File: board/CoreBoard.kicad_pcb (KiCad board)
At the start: 2 copper layers, 121.4 x 88.9 mm, 98 parts, among them J1 RJ45_LED_Shielded, J2 768250002, Q1 AO3401A, Q10 AO3401A, Q11 AO3401A, Q2 AO3401A, Q3 AO3401A, Q4 AO3401A, Q5 AO3401A, Q6 AO3401A, Q7 AO3401A, Q8 AO3401A, Q9 AO3401A, SW11 SW_Wuerth_450301014042, SW12 SW_Wuerth_450301014042, SW13 SW_Wuerth_450301014042, SW14 SW_Wuerth_450301014042, SW15 SW_Wuerth_450301014042, SW16 SW_Wuerth_450301014042, SW4 SW_Push, SW6 SW_Push, SW7 SW_Push, SW8 SW_Push, U1 74VHC138FT, U2 OKI-78SR-12_1.0-W36H-C, U3 SHHD003A0A, U4 GY-521, U5 Teensy4.1_DEV-16771, U6 MCP9808-E/MS

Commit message: rev2 progress
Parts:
- removed R28, R29: 10k, Resistor_SMD:R_0603_1608Metric_Pad0.98x0.95mm_HandSolder
- removed U3: SHHD003A0A, MRDT_Devices:SHHD003A0A-SRZ_Surface_Mount
- added C4: 10µF, Capacitor_SMD:C_1206_3216Metric_Pad1.33x1.80mm_HandSolder, F.Cu at (98.6, 91.4)
- added C5: 10µF, Capacitor_SMD:C_0603_1608Metric_Pad1.08x0.95mm_HandSolder, F.Cu at (97.7, 94.4)
- added Q1: AO3401A, Package_TO_SOT_SMD:SOT-23, F.Cu at (40.7, 78.7)
- added Q10: AO3401A, Package_TO_SOT_SMD:SOT-23, F.Cu at (50.5, 83.3)
- added Q12: AO3401A, Package_TO_SOT_SMD:SOT-23, F.Cu at (50.5, 87.9)
- added Q16: BSS138, Package_TO_SOT_SMD:SOT-23, F.Cu at (136.7, 121.5)
- added Q17: BSS138, Package_TO_SOT_SMD:SOT-23, F.Cu at (141.2, 121.9)
- added Q18: BSS138, Package_TO_SOT_SMD:SOT-23, F.Cu at (145.3, 121.9)
- added Q2: AO3401A, Package_TO_SOT_SMD:SOT-23, F.Cu at (40.7, 83.3)
- added Q3: AO3401A, Package_TO_SOT_SMD:SOT-23, F.Cu at (40.7, 87.9)
- added Q4: AO3401A, Package_TO_SOT_SMD:SOT-23, F.Cu at (40.7, 92.6)
- added Q5: AO3401A, Package_TO_SOT_SMD:SOT-23, F.Cu at (45.6, 78.7)
- added Q6: AO3401A, Package_TO_SOT_SMD:SOT-23, F.Cu at (45.6, 83.3)
- added Q7: AO3401A, Package_TO_SOT_SMD:SOT-23, F.Cu at (45.6, 87.9)
- added Q8: AO3401A, Package_TO_SOT_SMD:SOT-23, F.Cu at (45.6, 92.6)
- added Q9: AO3401A, Package_TO_SOT_SMD:SOT-23, F.Cu at (50.5, 78.7)
- added R17: 10k, Resistor_SMD:R_0603_1608Metric_Pad0.98x0.95mm_HandSolder, F.Cu at (138.8, 117.3)
- added R19: 10k, Resistor_SMD:R_0603_1608Metric_Pad0.98x0.95mm_HandSolder, F.Cu at (141.3, 117.3)
- added U7: OKI-78SR-5_1.5-W36H-C, Converter_DCDC:Converter_DCDC_Murata_OKI-78SR_Horizontal, F.Cu at (89.8, 89.9)
- MOSFET1: footprint MRDT_Devices:SOP-8_TOS-L -> CoreBoard:MSOP8_MC_MCH-L
- R27: value 6.8k -> 10k
- moved H4 21.8 mm to (168.7, 135.6)
- moved R16 5.24 mm to (192.0, 118.4)
- moved J1 5.11 mm to (181.5, 142.1)
- moved R27 2.17 mm to (143.8, 117.3)
- moved Conn9 1.55 mm to (144.3, 126.5)
- moved R14 1.05 mm to (192.0, 121.9)
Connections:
- Conn9 pad 1: /Fans/PWM2 -> +5V
- Conn9 pad 3: +12V -> Net-(Q17-D)
- Conn9 pad 4: GND -> Net-(Q18-D)
- R27 pad 1: /Fans/Tach2 -> /Lighting/BStrip
- U5 pad 33: unconnected-(U5-MCLK2-Pad33) -> /Lighting/GStrip
- U5 pad 4: /Fans/Tach2 -> /Lighting/RStrip
- U5 pad 9: /Fans/PWM2 -> /Lighting/BStrip
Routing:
- net /Lighting/GStrip: track 0.00 -> 211.0 mm, vias 0 -> 1
- net /Lighting/RStrip: track 0.00 -> 74.1 mm, vias 0 -> 5
- net /Lighting/BStrip: track 0.00 -> 70.6 mm, vias 0 -> 5
- net /Fans/PWM2: track 68.1 -> 0.00 mm, vias 5 -> 0
- net /Fans/Tach2: track 54.8 -> 0.00 mm, vias 3 -> 0
- net Rx-: track 41.8 -> 69.2 mm
- net Net-(Q18-D): track 0.00 -> 23.8 mm, vias 0 -> 1
- net /Accelerometer/AccSDA: track 117.6 -> 96.9 mm, vias 4 -> 3
- net /Accelerometer/AccSCL: track 126.0 -> 105.5 mm, vias 3 -> 2
- net Net-(Q17-D): track 0.00 -> 19.3 mm, vias 0 -> 2
- net Rx+: track 41.7 -> 58.3 mm
- net VCC: track 60.2 -> 76.6 mm, vias 2 -> 5
- net +3.3V: track 401.1 -> 411.7 mm, vias 12 -> 11
- net Net-(Q16-D): track 12.7 -> 6.72 mm
- net Tx+: track 28.0 -> 33.6 mm, vias 0 -> 1
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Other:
- board text removed: "Fan2"

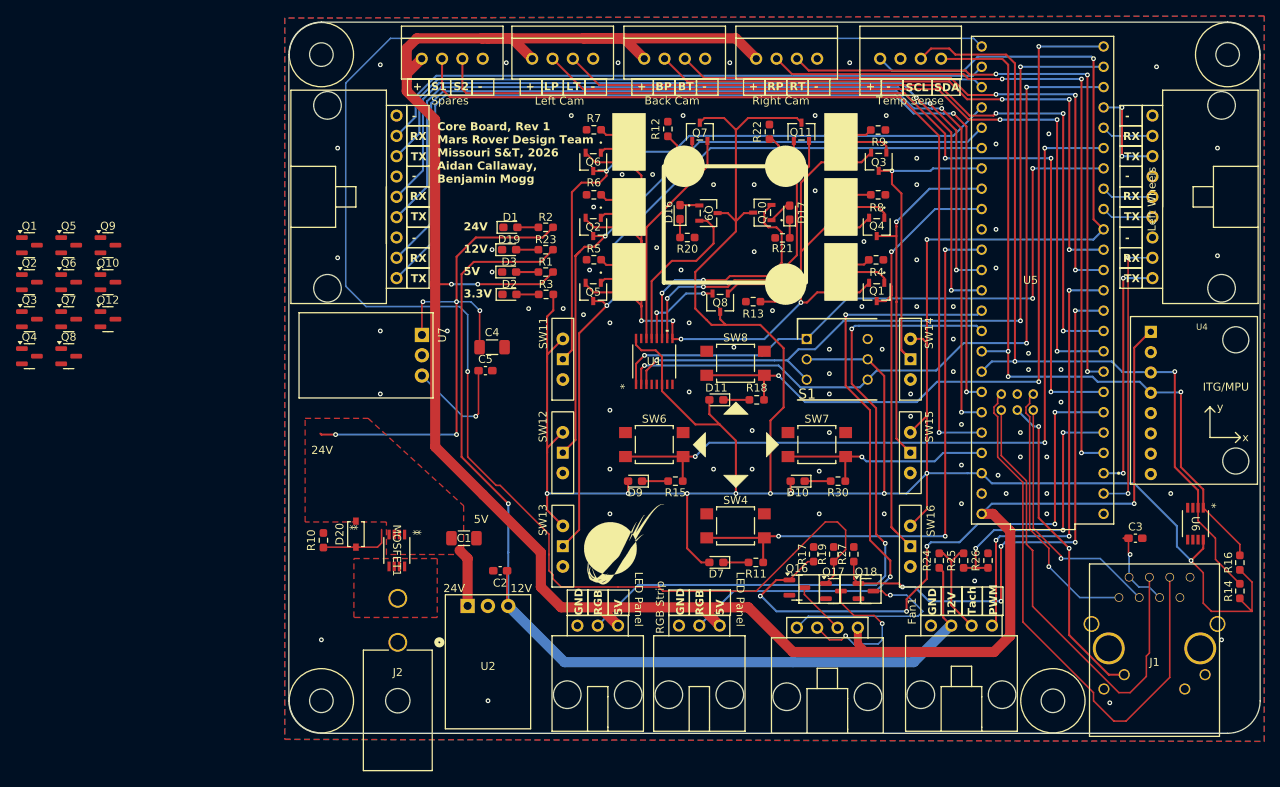
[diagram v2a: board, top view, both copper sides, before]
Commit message: move things for buck circuit
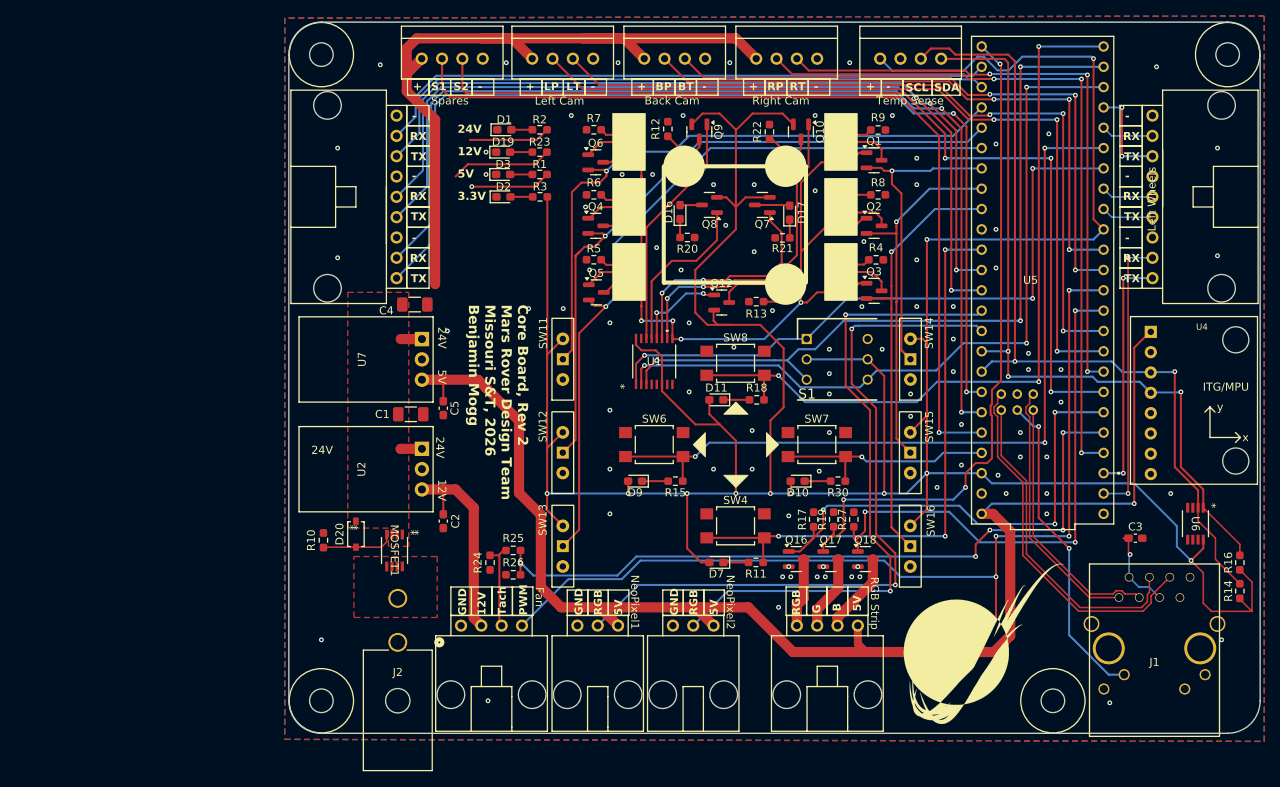
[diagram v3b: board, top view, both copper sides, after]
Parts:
- removed the G*** at (115.1, 116.1)
- removed the Q1 at (146.6, 84.5)
- removed the Q10 at (132.3, 74.6)
- removed Q11: AO3401A, CoreBoard:SOT-23-3L_AOS-L
- removed the Q2 at (111.2, 76.4)
- removed the Q3 at (146.9, 68.2)
- removed the Q4 at (146.6, 76.4)
- removed the Q5 at (111.2, 84.5)
- removed the Q6 at (111.2, 68.3)
- removed the Q7 at (124.5, 64.5)
- removed the Q8 at (127.1, 85.9)
- removed the Q9 at (125.6, 74.7)
- added G***: LOGO, MRDT_Silkscreens:0_MRDT_Logo_20mm, F.Cu at (160.0, 128.5)
- moved Q1 106.1 mm to (146.3, 68.1)
- moved Q2 105.8 mm to (146.3, 76.3)
- moved Q3 105.6 mm to (146.3, 84.4)
- moved Q10 88.6 mm to (137.2, 64.5), turned to -90 degrees
- moved Q7 87.9 mm to (132.3, 73.7), turned to 180 degrees
- moved Q8 82.3 mm to (125.7, 73.7), turned to 180 degrees
- moved Q12 76.7 mm to (127.3, 85.9)
- moved Q9 75.3 mm to (124.5, 64.5), turned to -90 degrees
- moved Q4 72.6 mm to (111.5, 76.3)
- moved Q6 67.6 mm to (111.5, 68.3)
- moved Q5 66.2 mm to (111.6, 84.6)
- moved R26 59.4 mm to (101.2, 119.9), turned to 180 degrees
- moved Conn2 58.7 mm to (102.3, 126.2)
- moved R25 56.3 mm to (101.2, 116.8), turned to 0 degrees
- moved R24 56.1 mm to (98.3, 118.4)
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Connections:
- C5 pad 1: +12V -> +5V
- Conn9 pad 2: Net-(Q16-D) -> Net-(Q18-D)
- Conn9 pad 4: Net-(Q18-D) -> Net-(Q16-D)
- U7 pad 3: +12V -> +5V
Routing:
- net /Lighting/GStrip: track 211.0 -> 84.2 mm, vias 1 -> 3
- net +12V: track 143.8 -> 38.3 mm, vias 2 -> 0
- net /Fans/PWM1: track 55.3 -> 119.0 mm, vias 3 -> 4
- net VCC: track 76.6 -> 15.5 mm, vias 5 -> 0
- net /Fans/Tach1: track 35.1 -> 92.1 mm, vias 3 -> 5
- net Rx-: track 69.2 -> 45.6 mm
- net +3.3V: track 411.7 -> 430.6 mm
- net Rx+: track 58.3 -> 40.6 mm
- net /Lighting/RStrip: track 74.1 -> 60.3 mm, vias 5 -> 3
- net Net-(Q18-D): track 23.8 -> 10.1 mm, vias 1 -> 0
- net Net-(Q17-D): track 19.3 -> 9.41 mm, vias 2 -> 0
- net +5V: track 286.5 -> 277.7 mm, vias 3 -> 2
- net /Lighting/BStrip: track 70.6 -> 67.7 mm, vias 5 -> 3
- net /Lighting/Lighting_Panel: track 87.8 -> 90.2 mm
- net /Selection LEDs/Spare2: track 31.3 -> 29.1 mm
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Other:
- board text added: "B"
- board text added: "Core Board, Rev 2 Mars Rover Design Team Missouri S&T, 2026 Benjamin Mogg"
- board text added: "Fan"
- board text added: "G"
- board text added: "NeoPixel1"
- board text added: "NeoPixel2"
- board text removed: "Core Board, Rev 1 Mars Rover Design Team Missouri S&T, 2026 Aidan Callaway, Benjamin Mogg"
- board text removed: "Fan1"
- board text removed: "LED Panel"

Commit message: add athena silkscreen
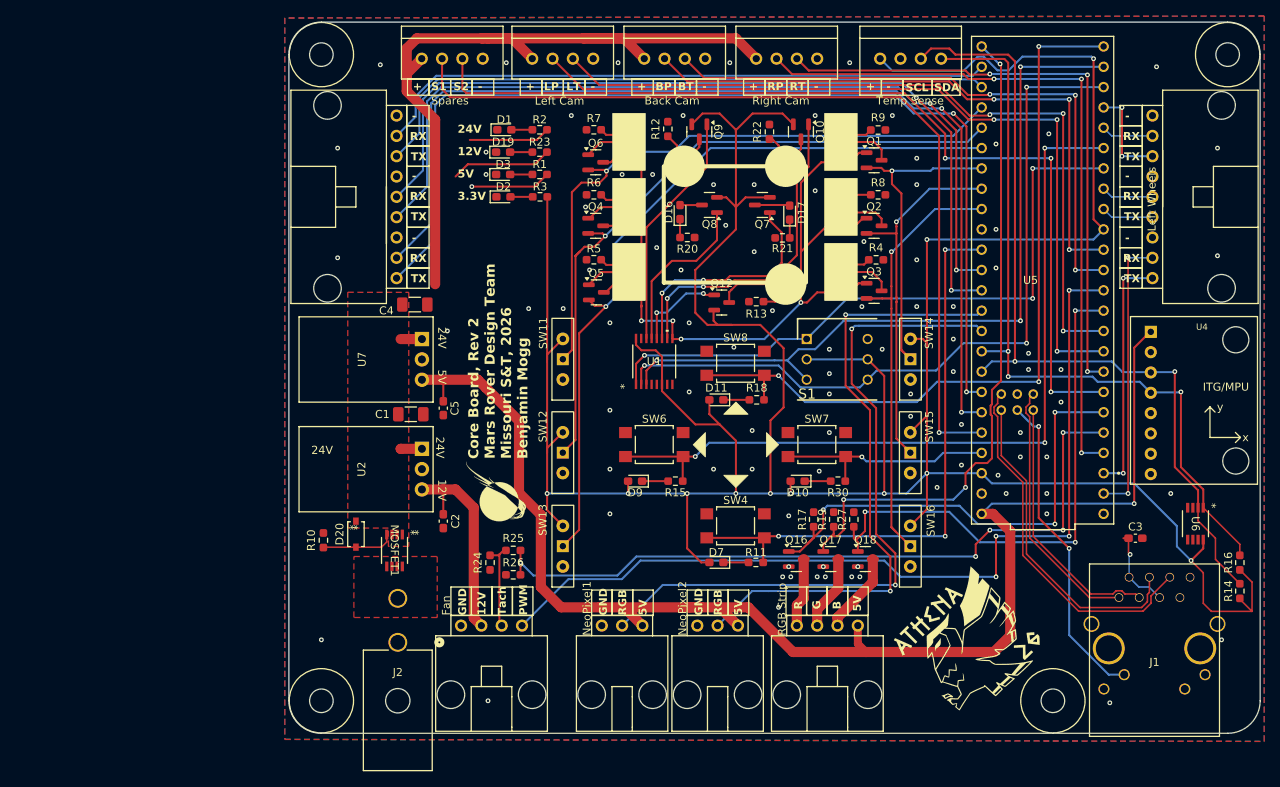
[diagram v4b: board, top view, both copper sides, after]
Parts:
- removed the G*** at (160.0, 128.5)
- added G***: LOGO, MRDT_Silkscreens:0_MRDT_Logo_7.5mm, F.Cu at (99.1, 109.5)
- added G***: LOGO, CoreBoard:Athena_Patch, F.Cu at (158.0, 128.5)
- moved Conn1 3.05 mm to (129.3, 126.2)
- moved Conn10 3.05 mm to (117.3, 126.2)
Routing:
- net /Fans/PWM1: track 119.0 -> 113.4 mm
- net /Lighting/RGB_Strip: track 80.5 -> 77.5 mm
- net /Lighting/Lighting_Panel: track 90.2 -> 87.2 mm
- net /Selection LEDs/Wheels: track 115.0 -> 114.1 mm
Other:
- board text added: "R"

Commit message: Add plated mounting holes and buck converter
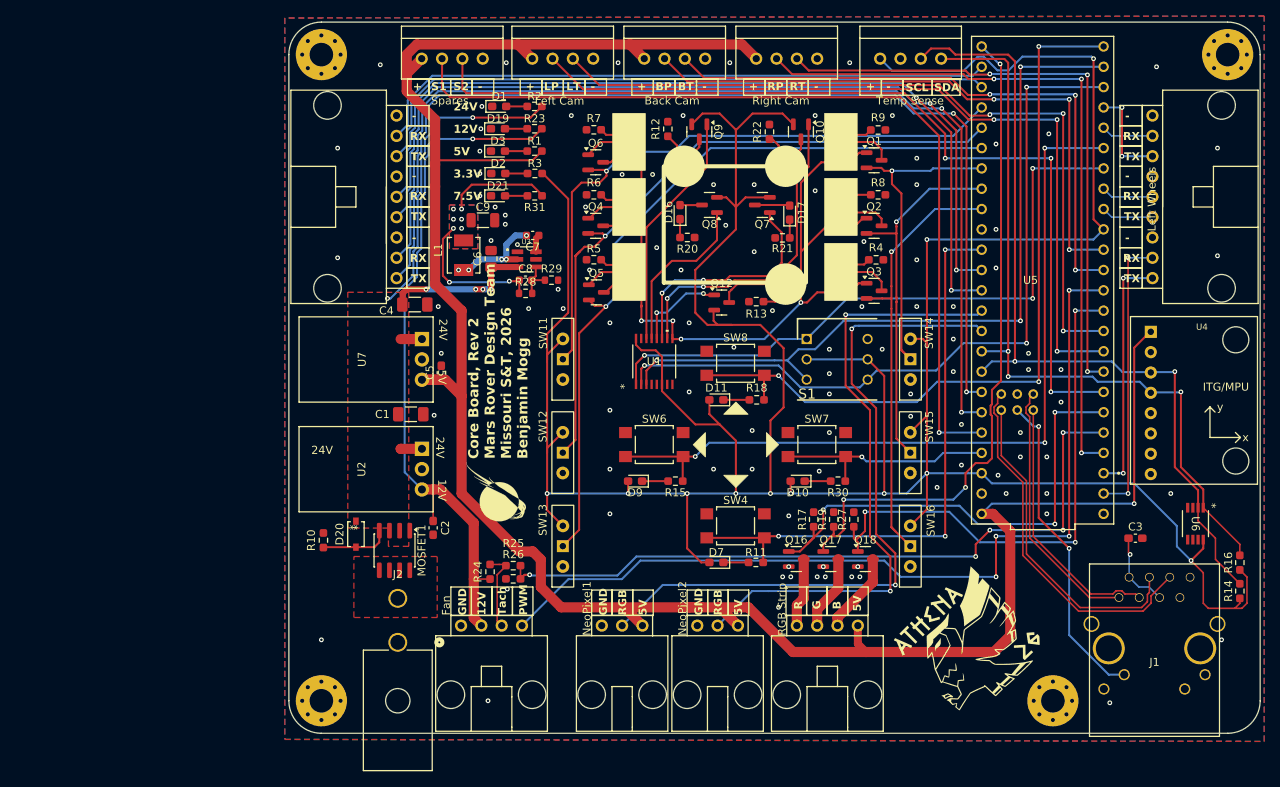
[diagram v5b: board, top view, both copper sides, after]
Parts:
- added C6: 15uF, Capacitor_SMD:C_0805_2012Metric_Pad1.18x1.45mm_HandSolder, F.Cu at (98.4, 80.4)
- added C7: 100nF, Capacitor_SMD:C_0603_1608Metric, F.Cu at (103.6, 77.5)
- added C8: 69pF, Capacitor_SMD:C_0603_1608Metric, F.Cu at (102.7, 83.1)
- added C9: 47uF, Capacitor_SMD:C_1206_3216Metric, F.Cu at (97.4, 75.6)
- added D21: Green, LED_SMD:LED_0603_1608Metric_Pad1.05x0.95mm_HandSolder, F.Cu at (99.3, 72.5)
- added L1: SRP4020TA-8R2M, CoreBoard:IND_SRP4020TA-8R2M, F.Cu at (95.0, 79.9)
- added R28: 100k, Resistor_SMD:R_0603_1608Metric, F.Cu at (102.7, 84.7)
- added R29: 8.66k, Resistor_SMD:R_0603_1608Metric, F.Cu at (106.0, 83.1)
- added R31: 1.5k, Resistor_SMD:R_0603_1608Metric_Pad0.98x0.95mm_HandSolder, F.Cu at (103.9, 72.5)
- added U3: TPS54202DDCR, CoreBoard:SOT95P280X110-6N, F.Cu at (102.9, 80.5)
- H1, H2, H3, H4: footprint MRDT_Drill_Holes:4_40_Hole -> MRDT_Drill_Holes:4_40_Hole_Pad_Via
- J2: footprint CoreBoard:CONN_SD-76825-0100_02_MOL -> MRDT_Connectors:MOLEX_MegaFit_02_Horizontal
- MOSFET1: footprint CoreBoard:MSOP8_MC_MCH-L -> Package_SO:SOIC-8_3.9x4.9mm_P1.27mm
- moved C5 4.45 mm to (92.2, 94.6), turned to 90 degrees
- moved D19 2.99 mm to (99.3, 64.1)
- moved R2 2.99 mm to (103.9, 61.3)
- moved R23 2.99 mm to (103.9, 64.1)
- moved D1 2.99 mm to (99.4, 61.3)
- moved D2 2.99 mm to (99.3, 69.7)
- moved R3 2.99 mm to (103.9, 69.7)
- moved D3 2.99 mm to (99.3, 66.9)
- moved R1 2.99 mm to (103.9, 66.9)
- moved R25 1.91 mm to (101.2, 118.7)
- moved C2 1.52 mm to (91.2, 114.0)
- moved R24 1.14 mm to (98.3, 119.5)
- moved R26 0.51 mm to (101.2, 120.4)
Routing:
- net +12V: track 38.3 -> 87.6 mm, vias 0 -> 1
- net VCC: track 15.5 -> 63.2 mm, vias 0 -> 6
- net +7.5V: track 0.00 -> 31.1 mm, vias 0 -> 8
- net Net-(U3-SW): track 0.00 -> 12.8 mm, vias 0 -> 5
- net +5V: track 277.7 -> 283.6 mm, vias 2 -> 1
- net Net-(U3-FB): track 0.00 -> 5.20 mm
- net +3.3V: track 430.6 -> 433.4 mm
- net Net-(D21-A): track 0.00 -> 2.80 mm
- net Net-(U3-BOOT): track 0.00 -> 2.19 mm
- net /Fans/Tach1: track 92.1 -> 90.2 mm
- net Net-(Conn2-Pad2): track 11.2 -> 10.2 mm
- net Net-(C3-Pad1): track 10.5 -> 9.88 mm
- net GND: vias 93 -> 105
- added copper zone on B.Cu, net +7.5V
- added copper zone on F.Cu, net +7.5V
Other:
- board text added: "7.5V"

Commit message: add voltage selection jumpers on servos
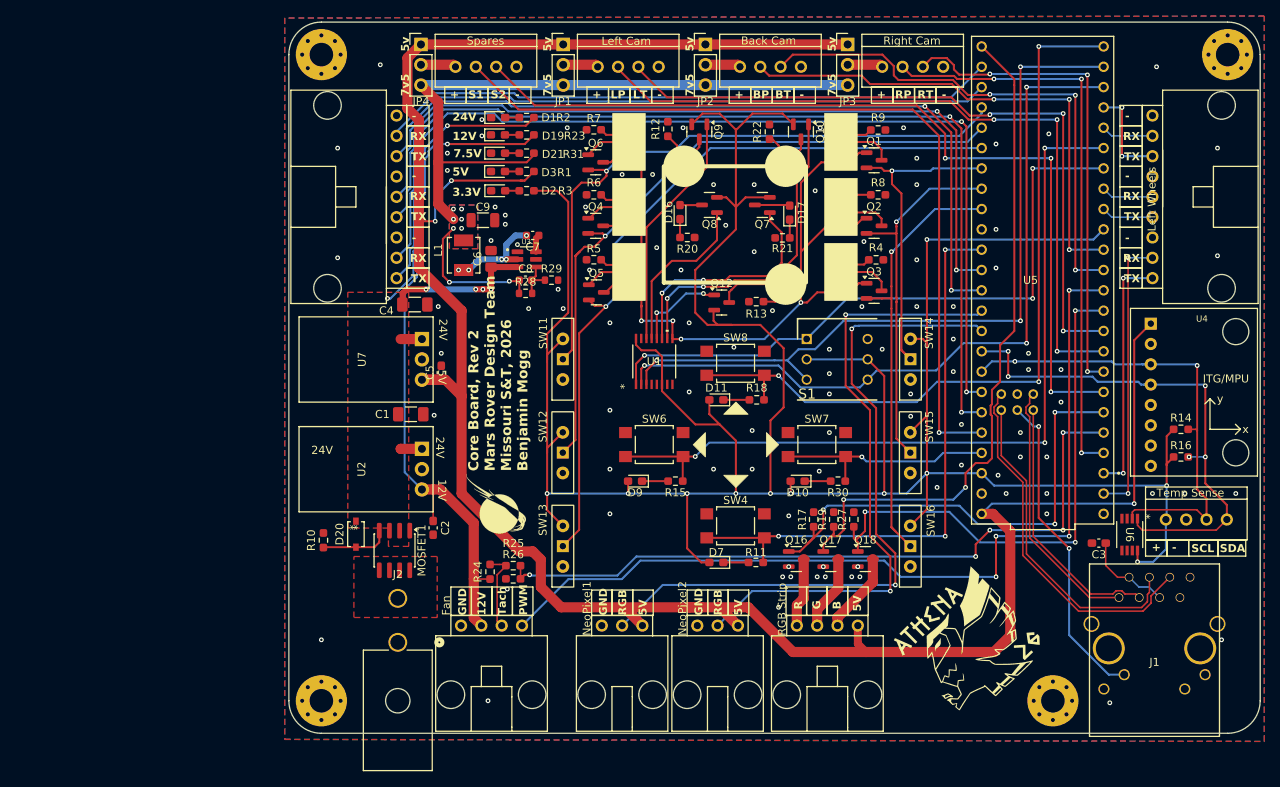
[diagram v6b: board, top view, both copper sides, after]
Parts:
- added JP1: Jumper_3_Bridged12, Connector_PinHeader_2.54mm:PinHeader_1x03_P2.54mm_Vertical, F.Cu at (107.4, 53.6)
- added JP2: Jumper_3_Bridged12, Connector_PinHeader_2.54mm:PinHeader_1x03_P2.54mm_Vertical, F.Cu at (125.2, 53.6)
- added JP3: Jumper_3_Bridged12, Connector_PinHeader_2.54mm:PinHeader_1x03_P2.54mm_Vertical, F.Cu at (143.0, 53.6)
- added JP4: Jumper_3_Bridged12, Connector_PinHeader_2.54mm:PinHeader_1x03_P2.54mm_Vertical, F.Cu at (89.7, 53.6)
- moved Conn11 67.8 mm to (182.8, 113.0)
- moved R14 21.5 mm to (184.7, 101.7), turned to 0 degrees
- moved Conn7 15.8 mm to (147.3, 56.4)
- moved R16 15.1 mm to (184.7, 105.2), turned to 0 degrees
- moved Conn6 12.0 mm to (129.5, 56.4)
- moved U6 8.33 mm to (178.3, 114.9)
- moved Conn5 8.25 mm to (111.8, 56.4)
- moved R31 5.43 mm to (102.9, 67.2)
- moved D21 5.33 mm to (99.3, 67.2)
- moved C3 4.61 mm to (174.4, 115.9), turned to 180 degrees
- moved Conn8 4.34 mm to (94.0, 56.4)
- moved R1 2.73 mm to (102.9, 69.5)
- moved D3 2.54 mm to (99.3, 69.5)
- moved R3 2.39 mm to (102.9, 71.9)
- moved D2 2.16 mm to (99.3, 71.9)
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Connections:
- Conn5 pad 1: +5V -> Net-(JP1-C)
- Conn6 pad 1: +5V -> Net-(JP2-C)
- Conn7 pad 1: +5V -> Net-(JP3-C)
- Conn8 pad 1: +5V -> Net-(JP4-C)
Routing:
- net +7.5V: track 31.1 -> 102.5 mm
- net +3.3V: track 433.4 -> 374.7 mm
- net /Accelerometer/AccSCL: track 105.6 -> 60.4 mm
- net /Accelerometer/AccSDA: track 97.1 -> 65.2 mm, vias 3 -> 5
- net /Gimbal Servos/RightPan: track 88.7 -> 72.5 mm
- net /Gimbal Servos/RightTilt: track 76.3 -> 61.4 mm
- net /Gimbal Servos/BackPan: track 75.8 -> 63.4 mm
- net /Gimbal Servos/BackTilt: track 76.1 -> 65.7 mm
- net /Gimbal Servos/LeftTilt: track 96.6 -> 88.1 mm
- net /Gimbal Servos/LeftPan: track 101.0 -> 92.5 mm
- net +5V: track 283.6 -> 291.6 mm, vias 1 -> 3
- net /Gimbal Servos/Spare2: track 118.5 -> 111.7 mm
- net /Gimbal Servos/Spare1: track 110.8 -> 103.9 mm
- net Net-(JP1-C): track 0.00 -> 4.42 mm
- net Net-(JP2-C): track 0.00 -> 4.42 mm
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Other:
- board text added: "5v"
- board text added: "7v5"
